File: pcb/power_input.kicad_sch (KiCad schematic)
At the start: 7 parts, among them J3 PJ-002B, J6 USB_C_Receptacle_USB2.0, U2 IP2721

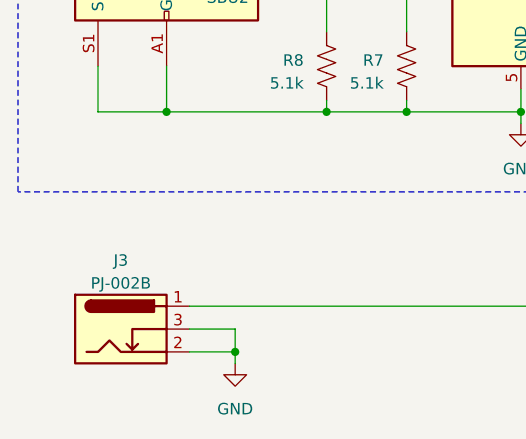
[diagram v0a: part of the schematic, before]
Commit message: fix incorrect part number in BOM
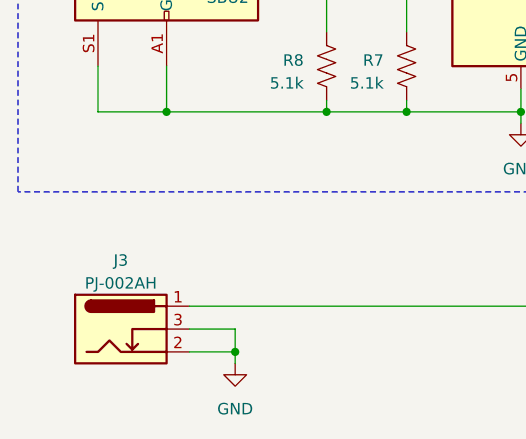
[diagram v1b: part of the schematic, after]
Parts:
- J3: value PJ-002B -> PJ-002AH; MPN PJ-002B -> PJ-002AH
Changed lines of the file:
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@@
 			)
 		)
-		(property "Value" "PJ-002B"
+		(property "Value" "PJ-002AH"
 			(at 109.22 120.65 0)
 			(effects
@@
 			)
 		)
-		(property "MPN" "PJ-002B"
+		(property "MPN" "PJ-002AH"
 			(at 109.22 125.73 0)
 			(effects
